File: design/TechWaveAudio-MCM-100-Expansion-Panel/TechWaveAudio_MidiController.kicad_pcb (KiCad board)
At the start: 2 copper layers, 10 x 128.5 mm, 0 parts

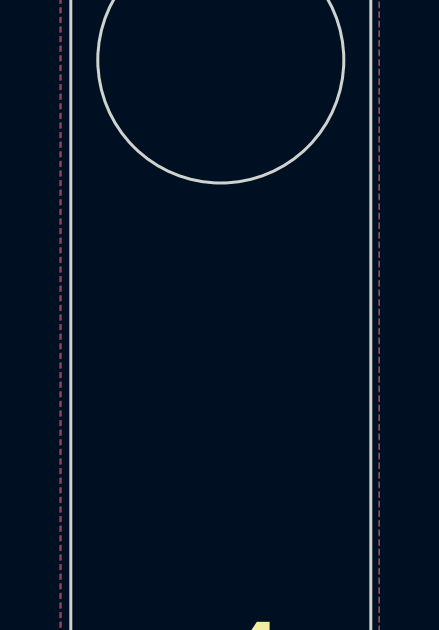
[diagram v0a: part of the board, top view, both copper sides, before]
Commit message: update expansion;  ensure ex state is properly set
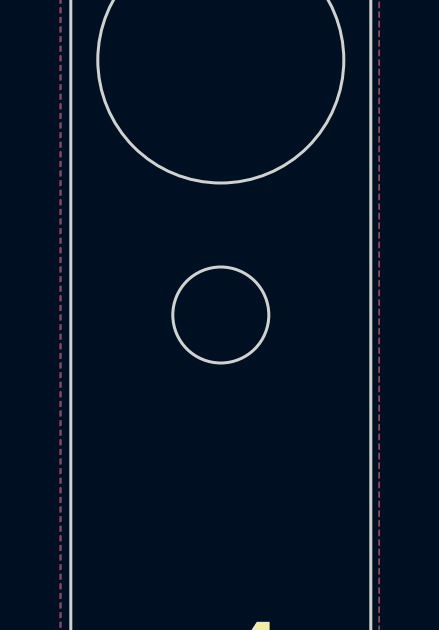
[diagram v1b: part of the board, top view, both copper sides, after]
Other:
- outline, holes or cut-outs redrawn
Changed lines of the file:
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@@
+	)
+	(gr_circle
+		(center 145.87 119.4)
+		(end 147.47 119.4)
+		(stroke
+			(width 0.1)
+			(type default)
+		)
+		(fill no)
+		(layer "Edge.Cuts")
 	)
 	(gr_circle
